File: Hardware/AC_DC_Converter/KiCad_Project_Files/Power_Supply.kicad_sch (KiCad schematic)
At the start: 12 parts

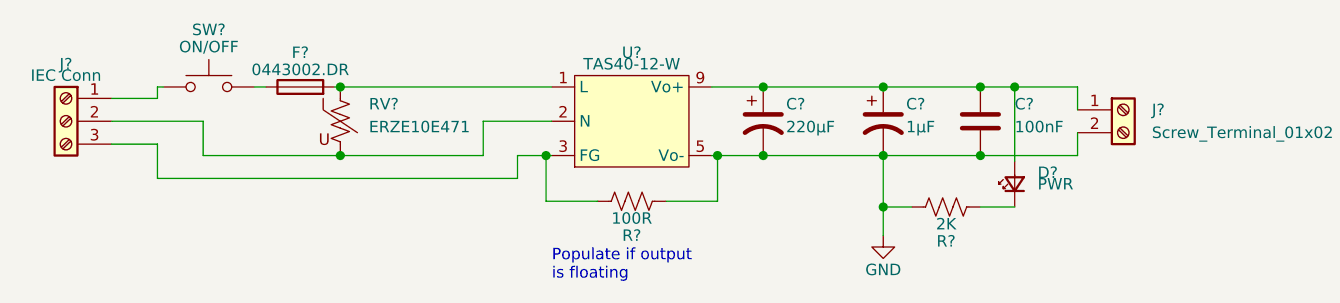
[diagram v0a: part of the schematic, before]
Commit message: changed input connector
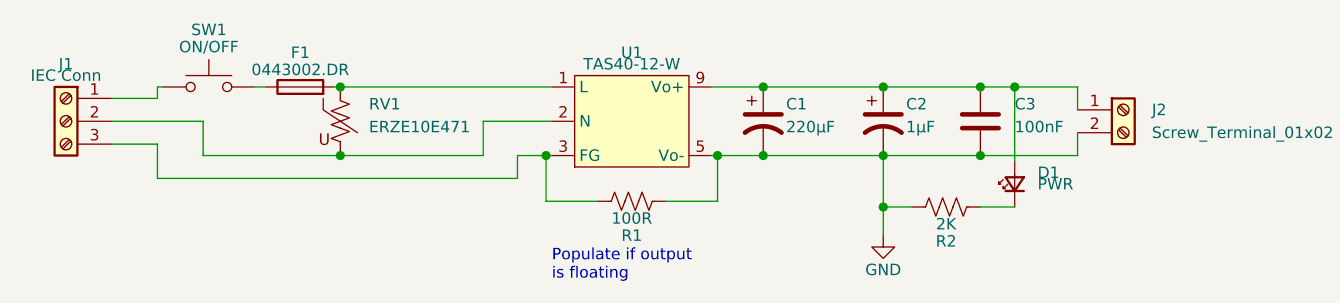
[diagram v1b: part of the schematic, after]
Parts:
- gave numbers to parts that had none: 12
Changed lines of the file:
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@@
   (symbol (lib_id "power:GND") (at 170.815 108.585 0) (unit 1)
     (in_bom yes) (on_board yes)
-    (property "Reference" "#PWR?" (id 0) (at 170.815 114.935 0)
+    (property "Reference" "#PWR0101" (id 0) (at 170.815 114.935 0)
       (effects (font (size 1.27 1.27)) hide)
     )
@@
   (symbol (lib_id "Device:Fuse") (at 106.045 92.075 90) (unit 1)
     (in_bom yes) (on_board yes)
-    (property "Reference" "F?" (id 0) (at 106.045 88.265 90))
+    (property "Reference" "F1" (id 0) (at 106.045 88.265 90))
     (property "Value" "0443002.DR" (id 1) (at 106.045 90.17 90))
     (property "Footprint" "Fuse:Fuse_2512_6332Metric_Castellated" (id 2) (at 106.045 93.853 90)
@@
   (symbol (lib_id "Device:R_US") (at 142.875 104.775 270) (unit 1)
     (in_bom yes) (on_board yes)
-    (property "Reference" "R?" (id 0) (at 142.875 108.585 90))
+    (property "Reference" "R1" (id 0) (at 142.875 108.585 90))
     (property "Value" "100R" (id 1) (at 142.875 106.68 90))
     (property "Footprint" "Resistor_SMD:R_0805_2012Metric" (id 2) (at 142.621 105.791 90)
@@
   (symbol (lib_id "Device:R_US") (at 177.8 105.41 270) (unit 1)
     (in_bom yes) (on_board yes)
-    (property "Reference" "R?" (id 0) (at 177.8 109.22 90))
+    (property "Reference" "R2" (id 0) (at 177.8 109.22 90))
     (property "Value" "2K" (id 1) (at 177.8 107.315 90))
     (property "Footprint" "Resistor_SMD:R_0805_2012Metric" (id 2) (at 177.546 106.426 90)
@@
   (symbol (lib_id "Device:LED_Small") (at 185.42 102.87 90) (unit 1)
     (in_bom yes) (on_board yes)
-    (property "Reference" "D?" (id 0) (at 187.96 101.6 90)
+    (property "Reference" "D1" (id 0) (at 187.96 101.6 90)
       (effects (font (size 1.27 1.27)) (justify right))
     )
@@
   (symbol (lib_id "Device:Varistor_US") (at 110.49 95.885 0) (unit 1)
     (in_bom yes) (on_board yes)
-    (property "Reference" "RV?" (id 0) (at 113.665 93.98 0)
+    (property "Reference" "RV1" (id 0) (at 113.665 93.98 0)
       (effects (font (size 1.27 1.27)) (justify left))
     )
@@
   (symbol (lib_id "Connector:Screw_Terminal_01x02") (at 197.485 94.615 0) (unit 1)
     (in_bom yes) (on_board yes)
-    (property "Reference" "J?" (id 0) (at 200.66 94.615 0)
+    (property "Reference" "J2" (id 0) (at 200.66 94.615 0)
       (effects (font (size 1.27 1.27)) (justify left))
     )
@@
   (symbol (lib_id "Device:CP1") (at 157.48 95.885 0) (unit 1)
     (in_bom yes) (on_board yes)
-    (property "Reference" "C?" (id 0) (at 160.02 93.98 0)
+    (property "Reference" "C1" (id 0) (at 160.02 93.98 0)
       (effects (font (size 1.27 1.27)) (justify left))
     )
@@
   (symbol (lib_id "Device:CP1") (at 170.815 95.885 0) (unit 1)
     (in_bom yes) (on_board yes)
-    (property "Reference" "C?" (id 0) (at 173.355 93.98 0)
+    (property "Reference" "C2" (id 0) (at 173.355 93.98 0)
       (effects (font (size 1.27 1.27)) (justify left))
     )
@@
   (symbol (lib_id "Device:C") (at 181.61 95.885 0) (unit 1)
     (in_bom yes) (on_board yes)
-    (property "Reference" "C?" (id 0) (at 185.42 93.98 0)
+    (property "Reference" "C3" (id 0) (at 185.42 93.98 0)
       (effects (font (size 1.27 1.27)) (justify left))
     )
@@
   (symbol (lib_id "Switch:SW_Push") (at 95.885 92.075 0) (unit 1)
     (in_bom yes) (on_board yes)
-    (property "Reference" "SW?" (id 0) (at 95.885 85.725 0))
+    (property "Reference" "SW1" (id 0) (at 95.885 85.725 0))
     (property "Value" "ON/OFF" (id 1) (at 95.885 87.63 0))
     (property "Footprint" "BPT_Switch:BPT" (id 2) (at 95.885 86.995 0)
@@
   (symbol (lib_id "Connector:Screw_Terminal_01x03") (at 80.01 95.885 0) (mirror y) (unit 1)
     (in_bom yes) (on_board yes)
-    (property "Reference" "J?" (id 0) (at 80.01 89.535 0))
+    (property "Reference" "J1" (id 0) (at 80.01 89.535 0))
     (property "Value" "IEC Conn" (id 1) (at 80.01 90.805 0))
     (property "Footprint" "IEC_Conn:ACT3KD-03BT3B018" (id 2) (at 80.01 95.885 0)
@@
   (symbol (lib_id "TAS30-12-W:TAS40-12-W") (at 142.875 95.885 0) (unit 1)
     (in_bom yes) (on_board yes)
-    (property "Reference" "U?" (id 0) (at 142.875 88.265 0))
+    (property "Reference" "U1" (id 0) (at 142.875 88.265 0))
     (property "Value" "TAS40-12-W" (id 1) (at 142.875 89.535 0))
     (property "Footprint" "TAS40-12-W:TAS40-12-W" (id 2) (at 152.4 108.585 0)
@@
   (symbol_instances
     (path "/f7dfabc0-51c3-4ac4-b466-c8c899298b3b"
-      (reference "#PWR?") (unit 1)
+      (reference "#PWR0101") (unit 1)
     )
     (path "/a6ee0a04-e43b-48b9-a146-ab694f690013"
-      (reference "C?") (unit 1)
+      (reference "C1") (unit 1)
     )
     (path "/a8774537-6cec-450b-846d-9049a5cc0139"
-      (reference "C?") (unit 1)
+      (reference "C2") (unit 1)
     )
     (path "/e576448d-a878-446c-8f13-fdba24193f90"
-      (reference "C?") (unit 1)
+      (reference "C3") (unit 1)
     )
     (path "/8be509b5-cf13-42a0-82a2-4bc404501bd4"
-      (reference "D?") (unit 1)
+      (reference "D1") (unit 1)
     )
     (path "/3ab2160e-aa75-4cf5-9937-f978a3db9ae4"
-      (reference "F?") (unit 1)
+      (reference "F1") (unit 1)
+    )
+    (path "/7c373b3d-b3b0-42b6-949c-34595983935d"
+      (reference "J1") (unit 1)
     )
     (path "/09bc29c1-38fb-40e7-a3cf-ae525e610532"
-      (reference "J?") (unit 1)
-    )
-    (path "/7c373b3d-b3b0-42b6-949c-34595983935d"
-      (reference "J?") (unit 1)
+      (reference "J2") (unit 1)
     )
     (path "/55537fa9-2206-4a33-b348-0c5d31aba118"
-      (reference "R?") (unit 1)
+      (reference "R1") (unit 1)
     )
     (path "/a46754ab-b3bf-4404-bd06-20c9b70781de"
-      (reference "R?") (unit 1)
+      (reference "R2") (unit 1)
     )
     (path "/302f3ee6-e8d1-459e-aab4-4adc7d9a4f3f"
-      (reference "RV?") (unit 1)
+      (reference "RV1") (unit 1)
     )
     (path "/cf824ac4-ba5a-4e0e-a58a-5fa5372cce1e"
-      (reference "SW?") (unit 1)
+      (reference "SW1") (unit 1)
     )
     (path "/08b297f9-2830-4094-86fb-7e1bbd933686"
-      (reference "U?") (unit 1)
-    )
-  )
+      (reference "U1") (unit 1)
+    )
+  )

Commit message: ac-dc layout complete and added 3d models
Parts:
- added H1, H3, H4: MountingHole, MountingHole:MountingHole_2.2mm_M2_DIN965_Pad, symbol Mechanical:MountingHole
- added H2: Earth, MountingHole:MountingHole_2.2mm_M2_DIN965_Pad, symbol Mechanical:MountingHole_Pad
- F1: footprint Fuse:Fuse_2512_6332Metric_Castellated -> Custom_Fuses:LittleFuse-0443002
- J2: footprint TerminalBlock_RND:TerminalBlock_RND_205-00287_1x02_P5.08mm_Horizontal -> TerminalBlock_Altech:Altech_AK300_1x02_P5.00mm_45-Degree
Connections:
- net Earth: now reaches J1.3 (Pin_3), R1.2, U1.3 (FG)
- net Earth: now also H2.1
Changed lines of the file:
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@@
   (page 1 1)
   (paper "A4")
+  (junction (at 93.98 102.235) (diameter 1.016) (color 0 0 0 0))
   (junction (at 110.49 92.075) (diameter 1.016) (color 0 0 0 0))
   (junction (at 110.49 99.695) (diameter 1.016) (color 0 0 0 0))
@@
     (stroke (width 0) (type solid) (color 0 0 0 0))
   )
-  (wire (pts (xy 90.17 102.235) (xy 130.175 102.235))
+  (wire (pts (xy 90.17 102.235) (xy 93.98 102.235))
+    (stroke (width 0) (type solid) (color 0 0 0 0))
+  )
+  (wire (pts (xy 93.98 102.235) (xy 93.98 108.585))
+    (stroke (width 0) (type solid) (color 0 0 0 0))
+  )
+  (wire (pts (xy 93.98 102.235) (xy 130.175 102.235))
     (stroke (width 0) (type solid) (color 0 0 0 0))
   )
@@
     (effects (font (size 1.27 1.27)) (justify left bottom))
   )
+  (symbol (lib_id "power:Earth") (at 93.98 108.585 0) (unit 1)
+    (in_bom yes) (on_board yes)
+    (property "Reference" "#PWR0102" (id 0) (at 93.98 114.935 0)
+      (effects (font (size 1.27 1.27)) hide)
+    )
+    (property "Value" "Earth" (id 1) (at 93.98 112.395 0)
+      (effects (font (size 1.27 1.27)) hide)
+    )
+    (property "Footprint" "" (id 2) (at 93.98 108.585 0)
+      (effects (font (size 1.27 1.27)) hide)
+    )
+    (property "Datasheet" "~" (id 3) (at 93.98 108.585 0)
+      (effects (font (size 1.27 1.27)) hide)
+    )
+  )
   (symbol (lib_id "power:GND") (at 170.815 108.585 0) (unit 1)
     (in_bom yes) (on_board yes)
@@
     )
   )
+  (symbol (lib_id "power:Earth") (at 226.695 147.32 0) (unit 1)
+    (in_bom yes) (on_board yes)
+    (property "Reference" "#PWR0103" (id 0) (at 226.695 153.67 0)
+      (effects (font (size 1.27 1.27)) hide)
+    )
+    (property "Value" "Earth" (id 1) (at 226.695 151.13 0)
+      (effects (font (size 1.27 1.27)) hide)
+    )
+    (property "Footprint" "" (id 2) (at 226.695 147.32 0)
+      (effects (font (size 1.27 1.27)) hide)
+    )
+    (property "Datasheet" "~" (id 3) (at 226.695 147.32 0)
+      (effects (font (size 1.27 1.27)) hide)
+    )
+  )
+  (symbol (lib_id "Mechanical:MountingHole") (at 226.695 137.16 0) (unit 1)
+    (in_bom yes) (on_board yes)
+    (property "Reference" "H1" (id 0) (at 229.87 137.16 0)
+      (effects (font (size 1.27 1.27)) (justify left))
+    )
+    (property "Value" "MountingHole" (id 1) (at 229.87 137.16 0)
+      (effects (font (size 1.27 1.27)) (justify left) hide)
+    )
+    (property "Footprint" "MountingHole:MountingHole_2.2mm_M2_DIN965_Pad" (id 2) (at 226.695 137.16 0)
+      (effects (font (size 1.27 1.27)) hide)
+    )
+    (property "Datasheet" "~" (id 3) (at 226.695 137.16 0)
+      (effects (font (size 1.27 1.27)) hide)
+    )
+  )
+  (symbol (lib_id "Mechanical:MountingHole") (at 236.855 137.16 0) (unit 1)
+    (in_bom yes) (on_board yes)
+    (property "Reference" "H3" (id 0) (at 240.03 137.16 0)
+      (effects (font (size 1.27 1.27)) (justify left))
+    )
+    (property "Value" "MountingHole" (id 1) (at 240.03 137.16 0)
+      (effects (font (size 1.27 1.27)) (justify left) hide)
+    )
+    (property "Footprint" "MountingHole:MountingHole_2.2mm_M2_DIN965_Pad" (id 2) (at 236.855 137.16 0)
+      (effects (font (size 1.27 1.27)) hide)
+    )
+    (property "Datasheet" "~" (id 3) (at 236.855 137.16 0)
+      (effects (font (size 1.27 1.27)) hide)
+    )
+  )
+  (symbol (lib_id "Mechanical:MountingHole") (at 236.855 143.51 0) (unit 1)
+    (in_bom yes) (on_board yes)
+    (property "Reference" "H4" (id 0) (at 240.03 143.51 0)
+      (effects (font (size 1.27 1.27)) (justify left))
+    )
+    (property "Value" "MountingHole" (id 1) (at 240.03 143.51 0)
+      (effects (font (size 1.27 1.27)) (justify left) hide)
+    )
+    (property "Footprint" "MountingHole:MountingHole_2.2mm_M2_DIN965_Pad" (id 2) (at 236.855 143.51 0)
+      (effects (font (size 1.27 1.27)) hide)
+    )
+    (property "Datasheet" "~" (id 3) (at 236.855 143.51 0)
+      (effects (font (size 1.27 1.27)) hide)
+    )
+  )
   (symbol (lib_id "Device:Fuse") (at 106.045 92.075 90) (unit 1)
     (in_bom yes) (on_board yes)
     (property "Reference" "F1" (id 0) (at 106.045 88.265 90))
     (property "Value" "0443002.DR" (id 1) (at 106.045 90.17 90))
-    (property "Footprint" "Fuse:Fuse_2512_6332Metric_Castellated" (id 2) (at 106.045 93.853 90)
+    (property "Footprint" "Custom_Fuses:LittleFuse-0443002" (id 2) (at 106.045 93.853 90)
       (effects (font (size 1.27 1.27)) hide)
     )
@@
     )
   )
+  (symbol (lib_id "Mechanical:MountingHole_Pad") (at 226.695 144.78 0) (unit 1)
+    (in_bom yes) (on_board yes)
+    (property "Reference" "H2" (id 0) (at 229.87 143.51 0)
+      (effects (font (size 1.27 1.27)) (justify left))
+    )
+    (property "Value" "Earth" (id 1) (at 230.505 144.78 0)
+      (effects (font (size 1.27 1.27)) (justify left) hide)
+    )
+    (property "Footprint" "MountingHole:MountingHole_2.2mm_M2_DIN965_Pad" (id 2) (at 226.695 144.78 0)
+      (effects (font (size 1.27 1.27)) hide)
+    )
+    (property "Datasheet" "~" (id 3) (at 226.695 144.78 0)
+      (effects (font (size 1.27 1.27)) hide)
+    )
+  )
   (symbol (lib_id "Device:Varistor_US") (at 110.49 95.885 0) (unit 1)
     (in_bom yes) (on_board yes)
@@
       (effects (font (size 1.27 1.27)) (justify left))
     )
-    (property "Footprint" "TerminalBlock_RND:TerminalBlock_RND_205-00287_1x02_P5.08mm_Horizontal" (id 2) (at 197.485 94.615 0)
+    (property "Footprint" "TerminalBlock_Altech:Altech_AK300_1x02_P5.00mm_45-Degree" (id 2) (at 197.485 94.615 0)
       (effects (font (size 1.27 1.27)) hide)
     )
@@
       (reference "#PWR0101") (unit 1)
     )
+    (path "/ab902a8d-665f-480c-b9b4-8401a8e76398"
+      (reference "#PWR0102") (unit 1)
+    )
+    (path "/a8b87f48-968c-42e5-b219-427650a68206"
+      (reference "#PWR0103") (unit 1)
+    )
     (path "/a6ee0a04-e43b-48b9-a146-ab694f690013"
       (reference "C1") (unit 1)
@@
       (reference "F1") (unit 1)
     )
+    (path "/f1ec1c18-1624-4d3a-952e-dc6b846eb0bd"
+      (reference "H1") (unit 1)
+    )
+    (path "/aefcf3d3-2524-40fa-affe-5bf5d4cd1eeb"
+      (reference "H2") (unit 1)
+    )
+    (path "/1bbe6bf0-2eed-4282-9583-f496790a155e"
+      (reference "H3") (unit 1)
+    )
+    (path "/4425a680-3577-48f2-84c0-30e2bfe79a68"
+      (reference "H4") (unit 1)
+    )
     (path "/7c373b3d-b3b0-42b6-949c-34595983935d"

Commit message: gerber files updated
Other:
- title: (none) -> ADSEHGAL
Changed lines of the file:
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@@
   (page 1 1)
   (paper "A4")
+  (title_block
+    (title "ADSEHGAL")
+    (date "2020-09-06")
+    (rev "0.1")
+  )
   (junction (at 93.98 102.235) (diameter 1.016) (color 0 0 0 0))
   (junction (at 110.49 92.075) (diameter 1.016) (color 0 0 0 0))
